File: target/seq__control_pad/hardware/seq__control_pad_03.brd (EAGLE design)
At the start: 120 x 70 mm, 78 parts, among them IC1 MEGA48/88/168-AU, SW1 EC12E_SW

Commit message: seq__control_pad: hardware
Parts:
- added C1, C2: 0.1, rcl:C0805
- added C3, C4: 18pF, rcl:C0805
- added D12, D13, D14, D15, D16, D17, D18: (no value), diode:MINIMELF
- added LD1: (no value), led:DUOLED-A-5MM
- added PAD47, PAD48, PAD49, PAD50, PAD51, PAD52, PAD53, PAD54: WIREPAD1,6/0,8, wirepad:1,6/0,8
- added R1, R2, R3, R4, R5, R6, R7, R8, R9: (no value), rcl:R0805
- added T1, T2, T3, T4: (no value), transistor:SOT23-BEC
- moved PAD21 57.0 mm to (110.5, 69.8)
- moved PAD22 57.0 mm to (110.5, 56.2)
- moved PAD27 57.0 mm to (53.5, 69.8)
- moved PAD28 57.0 mm to (53.5, 56.2)
- moved S11 57.0 mm to (110.5, 63.0)
- moved S17 57.0 mm to (53.5, 63.0)
- moved D11 53.7 mm to (101.0, 58.5), turned to 270 degrees
- moved Q1 41.0 mm to (94.0, 31.5), turned to 270 degrees
- moved PAD23 19.0 mm to (91.5, 69.8)
- moved PAD24 19.0 mm to (91.5, 56.2)
- moved PAD25 19.0 mm to (72.5, 69.8)
- moved PAD26 19.0 mm to (72.5, 56.2)
- moved S13 19.0 mm to (91.5, 63.0)
- moved S15 19.0 mm to (72.5, 63.0)
- moved PAD41 3.00 mm to (69.0, 32.0)
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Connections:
- removed net AGND: IC1.21
- removed net N$25: IC1.17
- removed net N$30: IC1.11
- removed net N$31: IC1.9
- removed net N$32: IC1.10
- new net ADC6: IC1.19, PAD49.1
- new net ADC7: IC1.22, PAD48.1
- new net C0SEL: IC1.26, R4.1
- new net C1SEL: IC1.23, R1.1
- new net C2SEL: IC1.24, R2.1
- new net C3SEL: IC1.25, R3.1
- new net EA: IC1.10, SW1.A
- new net EB: IC1.9, SW1.B
- new net ES: IC1.11, SW1.E
- new net INT: IC1.17, PAD54.1
- new net N$1: D11.C, S11.3
- new net N$20: D13.C, S15.3
- new net N$21: D14.C, S17.3
- new net N$23: D15.C, S12.1
- new net O0: IC1.16, R5.1
- new net O1: IC1.15, R6.1
- new net O2: IC1.14, R7.1
- new net O3: IC1.13, R8.1
- new net O4: IC1.12, R9.1
- new net RESET: IC1.29, PAD47.1
- new net SCL: IC1.28, PAD51.1
- new net SDA: IC1.27, PAD50.1
- net C0: now also T4.C; no longer IC1.23
- net C1: now also T1.C
- net C2: now also LD1.CX, S11.1, S13.1, S15.1, S17.1, T2.C; no longer S11.3
- net C3: now also LD1.CR, S12.4, S14.4, S16.4, S18.4, T3.C
- net GND: now also C1.2, C2.2, C3.1, C4.1, IC1.21, PAD53.1, SW1.C, SW1.D, T1.E, T2.E, T3.E, T4.E
- net IR0: now also D15.A
- net IR1: now also D12.A, D16.A
- net IR2: now also D13.A, D17.A
- net IR3: now also D14.A, D18.A
- net N$19: now also D12.C, S13.3; no longer D11.C, S11.1
- net N$2: now also R1.2, T1.B; no longer IC1.24
- net N$3: now also R2.2, T2.B; no longer IC1.25
- net N$4: now also R3.2, T3.B; no longer IC1.26
- net N$6: now also D16.C, S14.1; no longer IC1.27
- net N$7: now also R4.2, T4.B; no longer IC1.28
- net N$8: now also D17.C, S16.1; no longer IC1.19
- net N$9: now also D18.C, S18.1; no longer IC1.22
- net OR0: now also R5.2; no longer IC1.16
- net OR1: now also R6.2; no longer IC1.15
- net OR2: now also R7.2; no longer IC1.14
- net OR3: now also R8.2; no longer IC1.13
- net OR4: now also LD1.A, R9.2; no longer IC1.12
- net VCC: now also C1.1, C2.1, IC1.18, IC1.20, PAD52.1
- net XTAL1: now also C4.2
- net XTAL2: now also C3.2
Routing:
- net C1: track 138.6 -> 284.9 mm
- net GND: track 0.00 -> 131.4 mm
- net C0: track 111.8 -> 235.5 mm, vias 0 -> 2
- net IR0: track 99.0 -> 198.0 mm, vias 2 -> 3
- net OR3: track 85.1 -> 179.8 mm, vias 0 -> 3
- net IR1: track 95.6 -> 189.7 mm, vias 0 -> 4
- net C3: track 60.0 -> 140.9 mm, vias 0 -> 2
- net IR2: track 81.8 -> 157.4 mm, vias 0 -> 4
- net OR2: track 92.5 -> 159.7 mm, vias 0 -> 4
- net IR3: track 104.0 -> 170.8 mm, vias 0 -> 4
- net C2: track 75.1 -> 141.9 mm, vias 0 -> 2
- net OR0: track 98.4 -> 158.2 mm, vias 0 -> 4
- net OR4: track 106.7 -> 148.6 mm
- net ES: track 0.00 -> 27.1 mm
- net VCC: track 0.00 -> 25.0 mm
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- added copper zone on layer 16, net GND

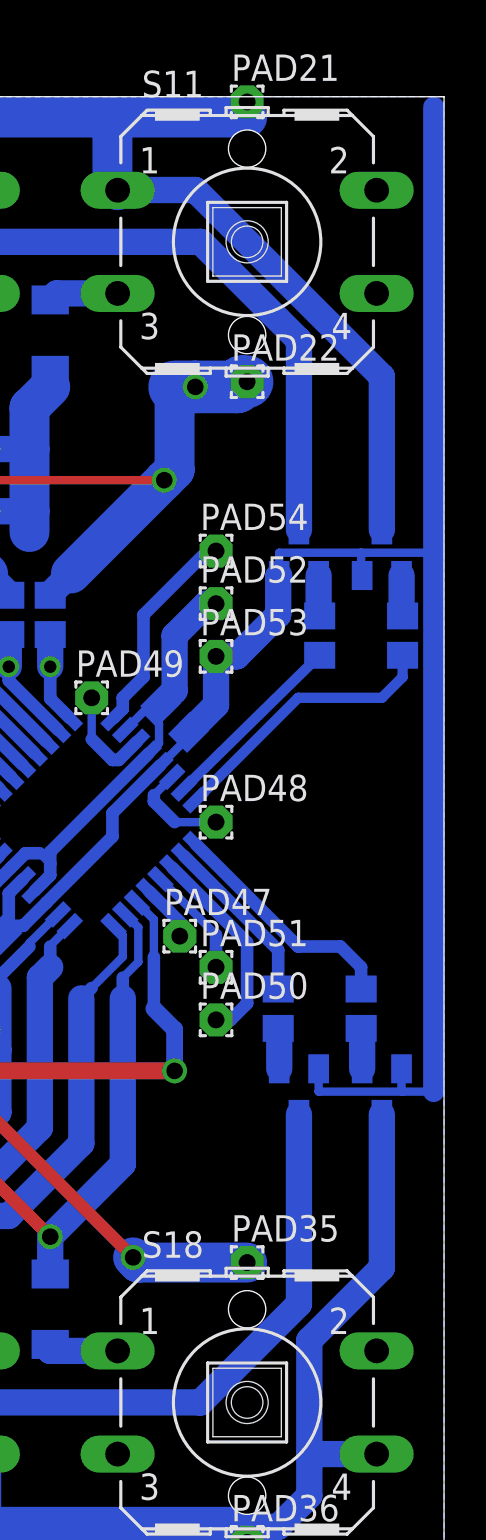
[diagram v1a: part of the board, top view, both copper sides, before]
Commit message: seq__control_pad_03.brd: updated layout
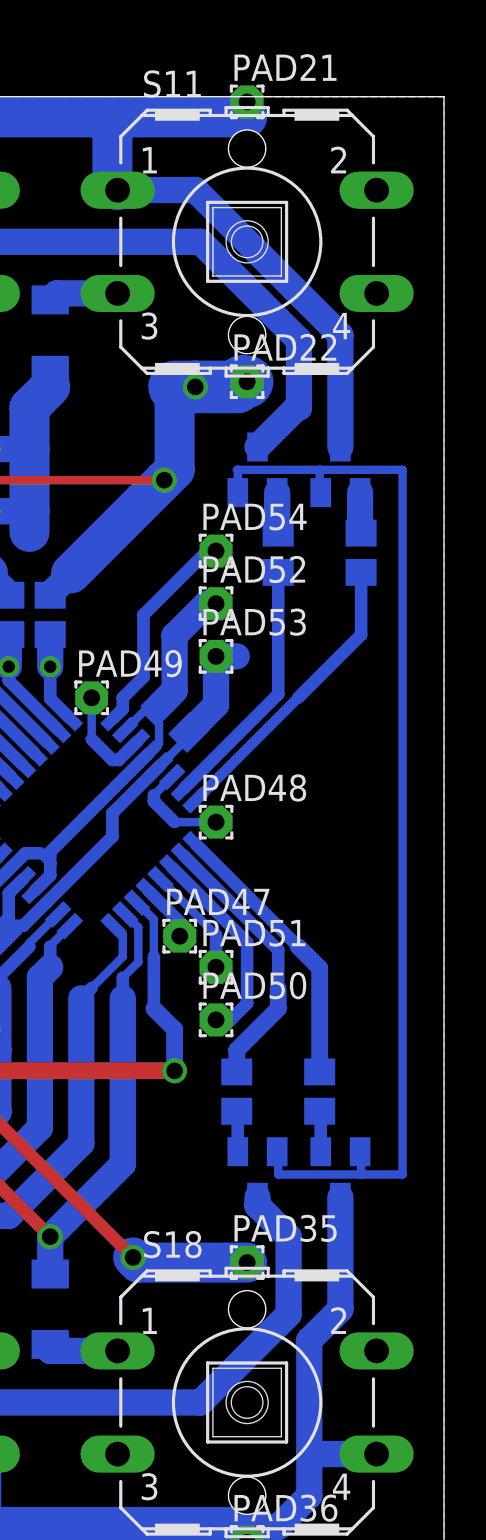
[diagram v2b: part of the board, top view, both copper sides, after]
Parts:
- moved R1 4.47 mm to (112.0, 48.0)
- moved R2 4.47 mm to (116.0, 48.0)
- moved R3 4.47 mm to (114.0, 22.0)
- moved R4 4.47 mm to (110.0, 22.0)
- moved T1 4.47 mm to (111.0, 52.0)
- moved T2 4.47 mm to (115.0, 52.0)
- moved T3 4.47 mm to (115.0, 18.0)
- moved T4 4.47 mm to (111.0, 18.0)
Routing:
- net GND: track 131.4 -> 114.2 mm
- net C3: track 140.9 -> 136.1 mm
- net C0SEL: track 8.31 -> 13.1 mm
- net C2: track 141.9 -> 137.1 mm
- net C0: track 235.5 -> 231.9 mm
- net C1SEL: track 9.18 -> 12.3 mm
- net C1: track 284.9 -> 281.8 mm
- net C3SEL: track 11.5 -> 13.5 mm
- net C2SEL: track 13.5 -> 14.3 mm
